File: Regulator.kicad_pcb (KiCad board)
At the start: 2 copper layers, 65 x 30.5 mm, 12 parts, among them J1 1x4 Header, J2 1X4 Header, J3 1x4 Header

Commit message: Cleanup files and component linkage errors
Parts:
- moved F1 0.13 mm to (120.4, 112.4)
- moved F2 0.13 mm to (159.2, 105.0)
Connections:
- net 12V Fuse renamed /12V Fuse
- net 5V Fuse renamed /5V Fuse
- net Bat Fuse renamed /Bat Fuse
- net Bat In renamed /Bat In
- net Comp Out renamed /Comp Out
- net NetD1_2 renamed Net-(D1-K)
- net NetD2_1 renamed Net-(D2-A)
- net NetD2_2 renamed Net-(D2-K)
- net NetD3_2 renamed Net-(D3-K)
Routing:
- net Net-(D2-A): track 0.53 -> 0.00 mm
- net GND: vias 5 -> 17
- net (no net): vias 4 -> 0
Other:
- rule pad_to_mask_clearance: 0 -> 0.05

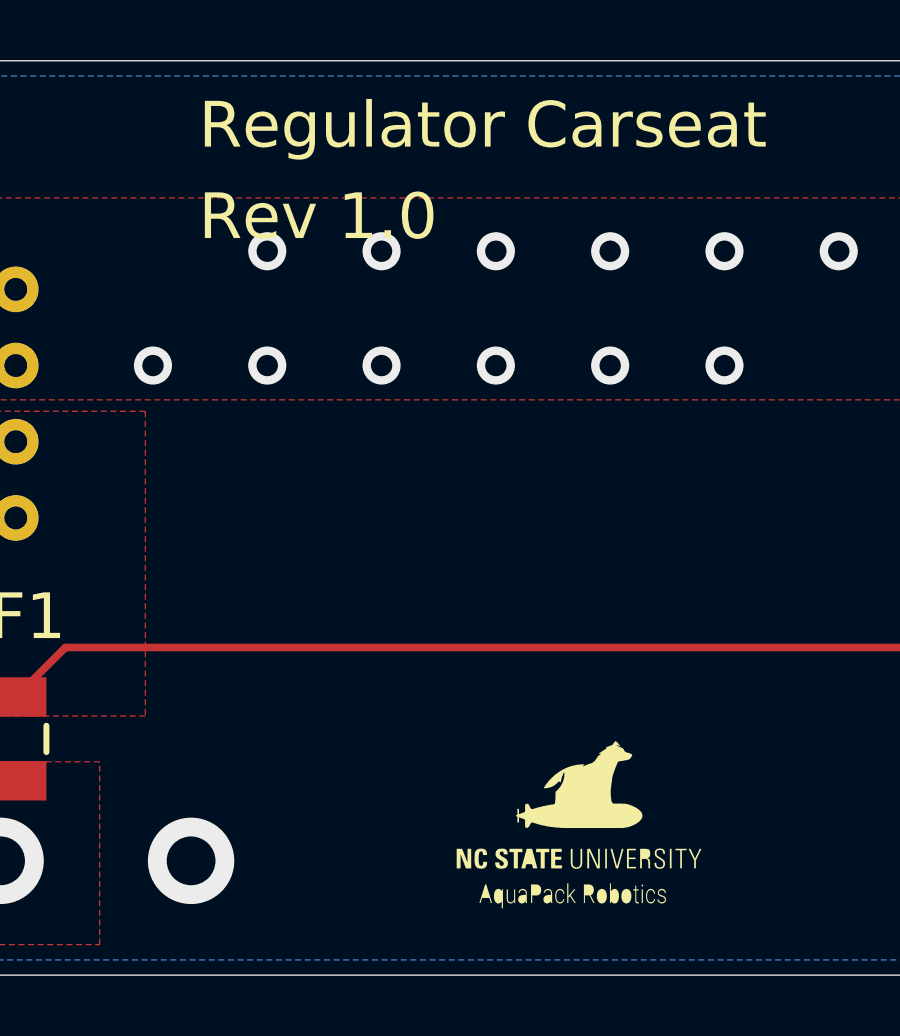
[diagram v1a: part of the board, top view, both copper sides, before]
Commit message: Fix silkscreen logos
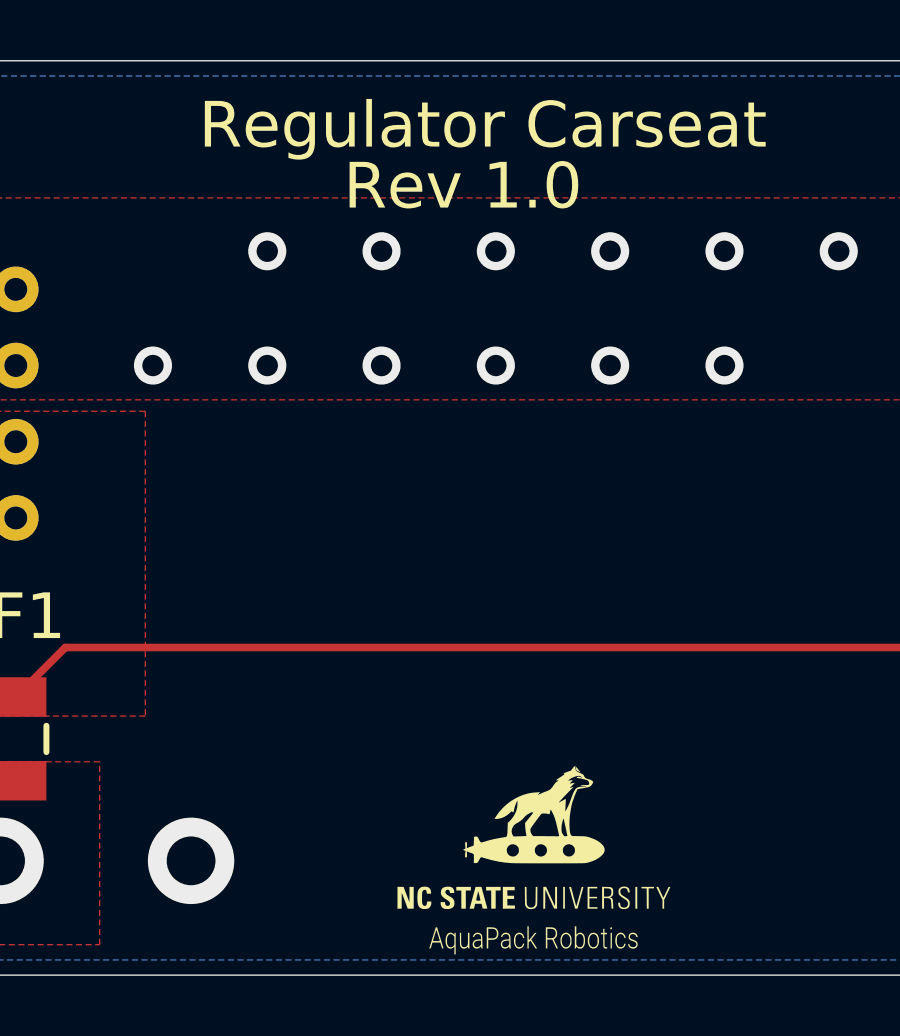
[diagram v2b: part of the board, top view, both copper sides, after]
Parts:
- added G***: LOGO, LOGO, F.Cu at (137.6, 116.4)
- added G***: LOGO, LOGO, B.Cu at (161.7, 115.2)
- added G***: LOGO, LOGO, B.Cu at (173.1, 115.2)

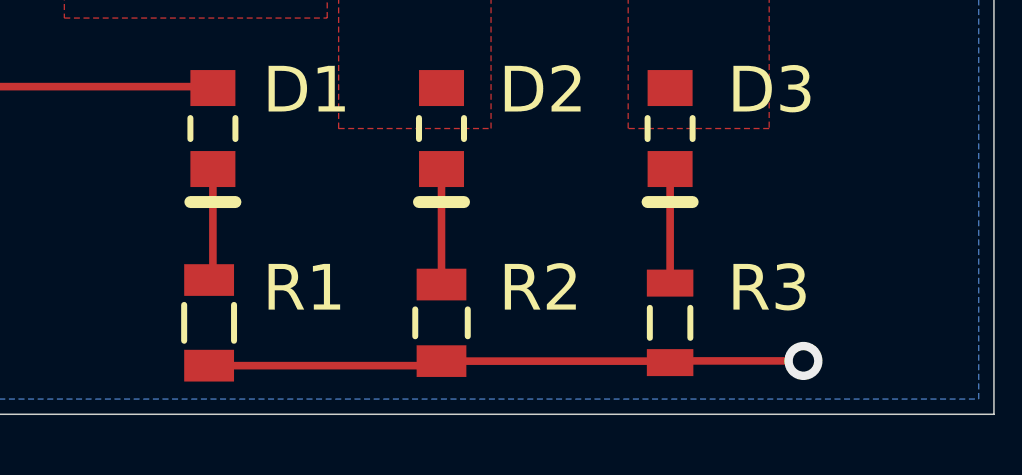
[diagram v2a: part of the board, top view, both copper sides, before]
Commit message: Cleanup component properties and footprints table
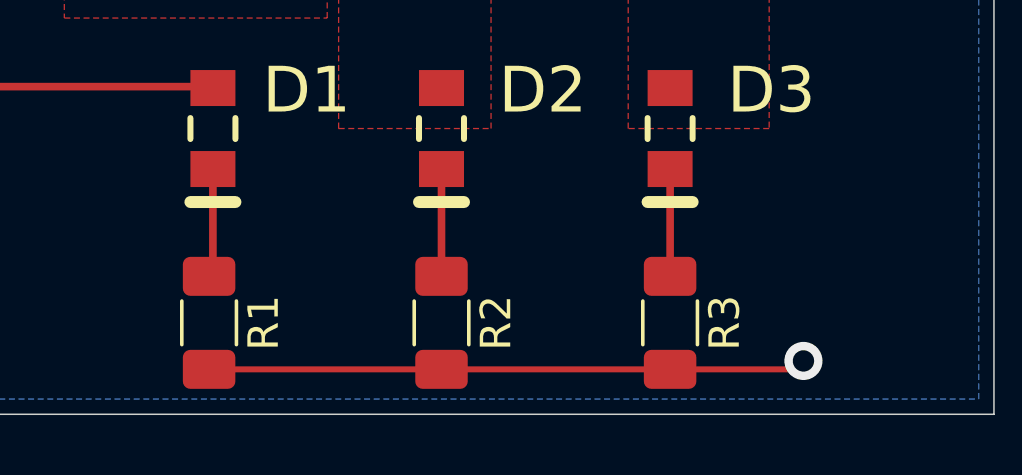
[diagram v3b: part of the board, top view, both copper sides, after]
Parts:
- R1: footprint AltiumImport:FP-CR1206-IPC_B -> Resistor_SMD:R_1206_3216Metric_Pad1.30x1.75mm_HandSolder
- R2: footprint AltiumImport:FP-MCA1206-IPC_C -> Resistor_SMD:R_1206_3216Metric_Pad1.30x1.75mm_HandSolder
- R3: footprint AltiumImport:RESC3216X70X50LL05T20 -> Resistor_SMD:R_1206_3216Metric_Pad1.30x1.75mm_HandSolder
